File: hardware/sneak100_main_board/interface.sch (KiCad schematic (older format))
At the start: 18 parts, among them J11 USB_OTG, J12 Conn_01x06, J13 Conn_01x02, SW2 SW_Push, U8 TSOP4838

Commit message: Add OLED display
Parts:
- removed J13: Conn_01x02, Connector_PinHeader_2.54mm:PinHeader_1x02_P2.54mm_Vertical, symbol Connector_Generic:Conn_01x02
- added C17, C18: 100nF, Capacitor_SMD:C_0603_1608Metric, symbol Device:C
- added R21, R22: 4k7, Resistor_SMD:R_0603_1608Metric, symbol Device:R
- added SW3, SW4: SW_Push, Button_Switch_SMD:SW_SPST_FSMSM, symbol Switch:SW_Push
- renumbered C17 to C19, R21 to R23, R22 to R24, R23 to R25, R24 to R26, R25 to R27, R26 to R28
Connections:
- wire segments 17 -> 29
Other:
- note added: "user buttons"
- note removed: "user button"
- moved on the sheet: C16, R20, SW2

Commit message: delete USB, modify top hull, bigger PCB board
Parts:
- removed D11: LED, LED_SMD:LED_0603_1608Metric, symbol Device:LED
- removed J11: USB_OTG, Connector_USB:USB_Mini-B_Lumberg_2486_01_Horizontal, symbol Connector:USB_OTG
- removed R23, R24: 300, Resistor_SMD:R_0603_1608Metric, symbol Device:R
- removed R27, R28: 22, Resistor_SMD:R_0603_1608Metric, symbol Device:R
- added J12: Conn_01x04, Connector_PinHeader_2.54mm:PinHeader_1x04_P2.54mm_Vertical, symbol Connector_Generic:Conn_01x04
- added R26: 340, Resistor_SMD:R_0603_1608Metric, symbol Device:R
- SW2, SW3, SW4: footprint Button_Switch_SMD:SW_SPST_FSMSM -> Button_Switch_SMD:SW_Push_1P1T_NO_6x6mm_H9.5mm
- renumbered C16 to C27, C17 to C28, C18 to C29, C19 to C30, J12 to J13, R19 to R22, R20 to R23, R21 to R24, R22 to R25, R25 to R27, R26 to R28, U8 to U9
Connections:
- net labels added: BUTTON_C, BUTTON_L, BUTTON_R, LED_ERROR, LED_RUN
- net labels removed: BUTTON, LED1, LED2, LED3, USB_DM, USB_DP
- wire segments 29 -> 25
- no-connect marks 5 -> 2
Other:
- note added: "Green led current resistor calculations:\n\ntarget current: I = 5mA\ninput voltage: U = 3.3V\nforward voltage: Uf = 2V\n\nR = (U-Uf)/I\nR = (3.3 -2)/0.005 = 260ohm -> 300ohm"
- note added: "HC-05 module"
- note added: "OLED display"
- note added: "Red led current resistor calculations:\n\ntarget current: I = 5mA\ninput voltage: U = 3.3V\nforward voltage: Uf = 1.6V\n\nR = (U-Uf)/I\nR = (3.3 -1.6)/0.005 = 340ohm"
- note added: "SSD1306 module"
- note added: "user led"
- note removed: "For future use:\n- IMU\n- OLED display"
- note removed: "Green led current resistor calculations:\n\ntarget current: I = 5mA\ninput voltage: U = 3.3V\nforward voltage: Uf = 2V\n\nR = (U-Uf)/I\nR = (3.3 -2.9)/0.005 = 260ohm -> 300ohm"
- note removed: "I2C bus"
- note removed: "USB connection"
- note removed: "user leds"
- moved on the sheet: C27, C29, R23, R25, SW2, SW4

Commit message: Board interface layout
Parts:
- removed J12: Conn_01x04, Connector_PinHeader_2.54mm:PinHeader_1x04_P2.54mm_Vertical, symbol Connector_Generic:Conn_01x04
- added U10: SSD1306, sneak100_lib:SSD1306_module, symbol Sneak100_kicad:SSD1306
- renumbered D9 to D7, D10 to D8, J13 to J12, R22 to R18, R23 to R19, R24 to R20, R25 to R21, R26 to R22, R27 to R23, R28 to R24
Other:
- note removed: "SSD1306 module"
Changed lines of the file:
@@
 $EndComp
 $Comp
-L Device:R R23
+L Device:R R19
 U 1 1 61055001
 P 1700 1700
-F 0 "R23" H 1770 1746 50  0000 L CNN
+F 0 "R19" H 1770 1746 50  0000 L CNN
 F 1 "4k7" H 1770 1655 50  0000 L CNN
 F 2 "Resistor_SMD:R_0603_1608Metric" V 1630 1700 50  0001 C CNN
@@
 $EndComp
 $Comp
-L power:+3.3V #PWR0114
+L power:+3.3V #PWR0109
 U 1 1 610558C1
 P 1700 1550
-F 0 "#PWR0114" H 1700 1400 50  0001 C CNN
+F 0 "#PWR0109" H 1700 1400 50  0001 C CNN
 F 1 "+3.3V" H 1715 1723 50  0000 C CNN
 F 2 "" H 1700 1550 50  0001 C CNN
@@
 $EndComp
 $Comp
-L power:GND #PWR0118
+L power:GND #PWR0113
 U 1 1 61055FD5
 P 1200 1950
-F 0 "#PWR0118" H 1200 1700 50  0001 C CNN
+F 0 "#PWR0113" H 1200 1700 50  0001 C CNN
 F 1 "GND" H 1205 1777 50  0000 C CNN
 F 2 "" H 1200 1950 50  0001 C CNN
@@
 $EndComp
 $Comp
-L power:GND #PWR0122
+L power:GND #PWR0117
 U 1 1 6105698D
 P 1700 2250
-F 0 "#PWR0122" H 1700 2000 50  0001 C CNN
+F 0 "#PWR0117" H 1700 2000 50  0001 C CNN
 F 1 "GND" H 1705 2077 50  0000 C CNN
 F 2 "" H 1700 2250 50  0001 C CNN
@@
 BUTTON_L
 $Comp
-L Device:LED D9
+L Device:LED D7
 U 1 1 6105F07D
 P 6450 1650
-F 0 "D9" H 6443 1395 50  0000 C CNN
+F 0 "D7" H 6443 1395 50  0000 C CNN
 F 1 "LED" H 6443 1486 50  0000 C CNN
 F 2 "LED_SMD:LED_0603_1608Metric" H 6450 1650 50  0001 C CNN
@@
 $EndComp
 $Comp
-L Device:R R22
+L Device:R R18
 U 1 1 61060DB0
 P 6150 1650
-F 0 "R22" V 5943 1650 50  0000 C CNN
+F 0 "R18" V 5943 1650 50  0000 C CNN
 F 1 "300" V 6034 1650 50  0000 C CNN
 F 2 "Resistor_SMD:R_0603_1608Metric" V 6080 1650 50  0001 C CNN
@@
 $EndComp
 $Comp
-L power:GND #PWR0117
+L power:GND #PWR0112
 U 1 1 61061E6F
 P 6600 1650
-F 0 "#PWR0117" H 6600 1400 50  0001 C CNN
+F 0 "#PWR0112" H 6600 1400 50  0001 C CNN
 F 1 "GND" V 6605 1522 50  0000 R CNN
 F 2 "" H 6600 1650 50  0001 C CNN
@@
 bluetooth module
 $Comp
-L Connector_Generic:Conn_01x06 J13
+L Connector_Generic:Conn_01x06 J12
 U 1 1 60F1EA00
 P 2350 6150
-F 0 "J13" H 2430 6142 50  0000 L CNN
+F 0 "J12" H 2430 6142 50  0000 L CNN
 F 1 "Conn_01x06" H 2430 6051 50  0000 L CNN
 F 2 "Connector_PinSocket_2.54mm:PinSocket_1x06_P2.54mm_Vertical" H 2350 6150 50  0001 C CNN
@@
 BLUETOOTH_TX
 $Comp
-L power:GND #PWR0133
+L power:GND #PWR0128
 U 1 1 60F1FEEB
 P 2150 6150
-F 0 "#PWR0133" H 2150 5900 50  0001 C CNN
+F 0 "#PWR0128" H 2150 5900 50  0001 C CNN
 F 1 "GND" V 2155 6022 50  0000 R CNN
 F 2 "" H 2150 6150 50  0001 C CNN
@@
 $EndComp
 $Comp
-L power:+5V #PWR0131
+L power:+5V #PWR0125
 U 1 1 60F200B0
 P 2150 6050
-F 0 "#PWR0131" H 2150 5900 50  0001 C CNN
+F 0 "#PWR0125" H 2150 5900 50  0001 C CNN
 F 1 "+5V" V 2165 6178 50  0000 L CNN
 F 2 "" H 2150 6050 50  0001 C CNN
@@
 Text Notes 5500 5500 0    100  ~ 20
 OLED display
-Text HLabel 5900 6300 0    50   BiDi ~ 0
+Text HLabel 6200 6050 1    50   BiDi ~ 0
 I2C_SDA
-Text HLabel 5900 6200 0    50   BiDi ~ 0
+Text HLabel 6100 6050 1    50   BiDi ~ 0
 I2C_SCL
 Text Notes 6200 3250 0    100  ~ 20
@@
 $EndComp
 $Comp
-L power:GND #PWR0129
+L power:GND #PWR0124
 U 1 1 60F7CCD5
 P 7150 4450
-F 0 "#PWR0129" H 7150 4200 50  0001 C CNN
+F 0 "#PWR0124" H 7150 4200 50  0001 C CNN
 F 1 "GND" H 7155 4277 50  0000 C CNN
 F 2 "" H 7150 4450 50  0001 C CNN
@@
 $EndComp
 $Comp
-L power:+3.3V #PWR0127
+L power:+3.3V #PWR0122
 U 1 1 60F7DC2F
 P 7450 3650
-F 0 "#PWR0127" H 7450 3500 50  0001 C CNN
+F 0 "#PWR0122" H 7450 3500 50  0001 C CNN
 F 1 "+3.3V" H 7465 3823 50  0000 C CNN
 F 2 "" H 7450 3650 50  0001 C CNN
@@
 $EndComp
 $Comp
-L power:GND #PWR0128
+L power:GND #PWR0123
 U 1 1 60F80FC7
 P 5900 3950
-F 0 "#PWR0128" H 5900 3700 50  0001 C CNN
+F 0 "#PWR0123" H 5900 3700 50  0001 C CNN
 F 1 "GND" H 5905 3777 50  0000 C CNN
 F 2 "" H 5900 3950 50  0001 C CNN
@@
 $EndComp
 $Comp
-L power:+3.3V #PWR0125
+L power:+3.3V #PWR0120
 U 1 1 60F81378
 P 5900 3650
-F 0 "#PWR0125" H 5900 3500 50  0001 C CNN
+F 0 "#PWR0120" H 5900 3500 50  0001 C CNN
 F 1 "+3.3V" H 5915 3823 50  0000 C CNN
 F 2 "" H 5900 3650 50  0001 C CNN
@@
 $EndComp
 $Comp
-L Device:R R27
+L Device:R R23
 U 1 1 60F8B46D
 P 7150 3800
-F 0 "R27" H 7220 3846 50  0000 L CNN
+F 0 "R23" H 7220 3846 50  0000 L CNN
 F 1 "100" H 7220 3755 50  0000 L CNN
 F 2 "Resistor_SMD:R_0603_1608Metric" V 7080 3800 50  0001 C CNN
@@
 $EndComp
 $Comp
-L power:+3.3V #PWR0126
+L power:+3.3V #PWR0121
 U 1 1 60F8BCE9
 P 7150 3650
-F 0 "#PWR0126" H 7150 3500 50  0001 C CNN
+F 0 "#PWR0121" H 7150 3500 50  0001 C CNN
 F 1 "+3.3V" H 7165 3823 50  0000 C CNN
 F 2 "" H 7150 3650 50  0001 C CNN
@@
 	7150 4400 7150 4450
 $Comp
-L Device:R R28
+L Device:R R24
 U 1 1 60F9B98E
 P 7450 3800
-F 0 "R28" H 7520 3846 50  0000 L CNN
+F 0 "R24" H 7520 3846 50  0000 L CNN
 F 1 "10k" H 7520 3755 50  0000 L CNN
 F 2 "Resistor_SMD:R_0603_1608Metric" V 7380 3800 50  0001 C CNN
@@
 $EndComp
 $Comp
-L Device:R R24
+L Device:R R20
 U 1 1 60F90EC5
 P 2900 1700
-F 0 "R24" H 2970 1746 50  0000 L CNN
+F 0 "R20" H 2970 1746 50  0000 L CNN
 F 1 "4k7" H 2970 1655 50  0000 L CNN
 F 2 "Resistor_SMD:R_0603_1608Metric" V 2830 1700 50  0001 C CNN
@@
 $EndComp
 $Comp
-L power:+3.3V #PWR0115
+L power:+3.3V #PWR0110
 U 1 1 60F90ECB
 P 2900 1550
-F 0 "#PWR0115" H 2900 1400 50  0001 C CNN
+F 0 "#PWR0110" H 2900 1400 50  0001 C CNN
 F 1 "+3.3V" H 2915 1723 50  0000 C CNN
 F 2 "" H 2900 1550 50  0001 C CNN
@@
 $EndComp
 $Comp
-L power:GND #PWR0119
+L power:GND #PWR0114
 U 1 1 60F90ED1
 P 2400 1950
-F 0 "#PWR0119" H 2400 1700 50  0001 C CNN
+F 0 "#PWR0114" H 2400 1700 50  0001 C CNN
 F 1 "GND" H 2405 1777 50  0000 C CNN
 F 2 "" H 2400 1950 50  0001 C CNN
@@
 $EndComp
 $Comp
-L power:GND #PWR0123
+L power:GND #PWR0118
 U 1 1 60F90EDD
 P 2900 2250
-F 0 "#PWR0123" H 2900 2000 50  0001 C CNN
+F 0 "#PWR0118" H 2900 2000 50  0001 C CNN
 F 1 "GND" H 2905 2077 50  0000 C CNN
 F 2 "" H 2900 2250 50  0001 C CNN
@@
 $EndComp
 $Comp
-L Device:R R25
+L Device:R R21
 U 1 1 60F92AB2
 P 4100 1700
-F 0 "R25" H 4170 1746 50  0000 L CNN
+F 0 "R21" H 4170 1746 50  0000 L CNN
 F 1 "4k7" H 4170 1655 50  0000 L CNN
 F 2 "Resistor_SMD:R_0603_1608Metric" V 4030 1700 50  0001 C CNN
@@
 $EndComp
 $Comp
-L power:+3.3V #PWR0116
+L power:+3.3V #PWR0111
 U 1 1 60F92AB8
 P 4100 1550
-F 0 "#PWR0116" H 4100 1400 50  0001 C CNN
+F 0 "#PWR0111" H 4100 1400 50  0001 C CNN
 F 1 "+3.3V" H 4115 1723 50  0000 C CNN
 F 2 "" H 4100 1550 50  0001 C CNN
@@
 $EndComp
 $Comp
-L power:GND #PWR0120
+L power:GND #PWR0115
 U 1 1 60F92ABE
 P 3600 1950
-F 0 "#PWR0120" H 3600 1700 50  0001 C CNN
+F 0 "#PWR0115" H 3600 1700 50  0001 C CNN
 F 1 "GND" H 3605 1777 50  0000 C CNN
 F 2 "" H 3600 1950 50  0001 C CNN
@@
 $EndComp
 $Comp
-L power:GND #PWR0124
+L power:GND #PWR0119
 U 1 1 60F92ACA
 P 4100 2250
-F 0 "#PWR0124" H 4100 2000 50  0001 C CNN
+F 0 "#PWR0119" H 4100 2000 50  0001 C CNN
 F 1 "GND" H 4105 2077 50  0000 C CNN
 F 2 "" H 4100 2250 50  0001 C CNN
@@
 BUTTON_R
 $Comp
-L Connector_Generic:Conn_01x04 J12
-U 1 1 60FBB3CA
-P 6100 6100
-F 0 "J12" H 6180 6092 50  0000 L CNN
-F 1 "Conn_01x04" H 6180 6001 50  0000 L CNN
-F 2 "Connector_PinHeader_2.54mm:PinHeader_1x04_P2.54mm_Vertical" H 6100 6100 50  0001 C CNN
-F 3 "~" H 6100 6100 50  0001 C CNN
-	1    6100 6100
-	1    0    0    -1
-$EndComp
-$Comp
-L power:+3.3V #PWR0130
+L power:+3.3V #PWR0126
 U 1 1 60FBF32E
-P 5900 6000
-F 0 "#PWR0130" H 5900 5850 50  0001 C CNN
-F 1 "+3.3V" V 5915 6128 50  0000 L CNN
-F 2 "" H 5900 6000 50  0001 C CNN
-F 3 "" H 5900 6000 50  0001 C CNN
-	1    5900 6000
-	0    -1   -1   0
-$EndComp
-$Comp
-L power:GND #PWR0132
+P 5900 6050
+F 0 "#PWR0126" H 5900 5900 50  0001 C CNN
+F 1 "+3.3V" V 5915 6178 50  0000 L CNN
+F 2 "" H 5900 6050 50  0001 C CNN
+F 3 "" H 5900 6050 50  0001 C CNN
+	1    5900 6050
+	1    0    0    -1
+$EndComp
+$Comp
+L power:GND #PWR0127
 U 1 1 60FBFC20
-P 5900 6100
-F 0 "#PWR0132" H 5900 5850 50  0001 C CNN
-F 1 "GND" V 5905 5972 50  0000 R CNN
-F 2 "" H 5900 6100 50  0001 C CNN
-F 3 "" H 5900 6100 50  0001 C CNN
-	1    5900 6100
-	0    1    1    0
-$EndComp
-$Comp
-L Device:LED D10
+P 6000 6050
+F 0 "#PWR0127" H 6000 5800 50  0001 C CNN
+F 1 "GND" V 6005 5922 50  0000 R CNN
+F 2 "" H 6000 6050 50  0001 C CNN
+F 3 "" H 6000 6050 50  0001 C CNN
+	1    6000 6050
+	-1   0    0    1
+$EndComp
+$Comp
+L Device:LED D8
 U 1 1 60FD241C
 P 6450 2100
-F 0 "D10" H 6443 1845 50  0000 C CNN
+F 0 "D8" H 6443 1845 50  0000 C CNN
 F 1 "LED" H 6443 1936 50  0000 C CNN
 F 2 "LED_SMD:LED_0603_1608Metric" H 6450 2100 50  0001 C CNN
@@
 $EndComp
 $Comp
-L Device:R R26
+L Device:R R22
 U 1 1 60FD2422
 P 6150 2100
-F 0 "R26" V 5943 2100 50  0000 C CNN
+F 0 "R22" V 5943 2100 50  0000 C CNN
 F 1 "340" V 6034 2100 50  0000 C CNN
 F 2 "Resistor_SMD:R_0603_1608Metric" V 6080 2100 50  0001 C CNN
@@
 $EndComp
 $Comp
-L power:GND #PWR0121
+L power:GND #PWR0116
 U 1 1 60FD2428
 P 6600 2100
-F 0 "#PWR0121" H 6600 1850 50  0001 C CNN
+F 0 "#PWR0116" H 6600 1850 50  0001 C CNN
 F 1 "GND" V 6605 1972 50  0000 R CNN
 F 2 "" H 6600 2100 50  0001 C CNN
@@
 Text Notes 7600 2550 0    50   ~ 0
 Red led current resistor calculations:\n\ntarget current: I = 5mA\ninput voltage: U = 3.3V\nforward voltage: Uf = 1.6V\n\nR = (U-Uf)/I\nR = (3.3 -1.6)/0.005 = 340ohm
-Text Notes 5650 5650 0    50   ~ 10
-SSD1306 module
 Text Notes 2000 5600 0    50   ~ 10
 HC-05 module
+$Comp
+L Sneak100_kicad:SSD1306 U10
+U 1 1 6101ACF5
+P 6050 6400
+F 0 "U10" H 6650 6750 50  0000 R CNN
+F 1 "SSD1306" H 6800 6650 50  0000 R CNN
+F 2 "sneak100_lib:SSD1306_module" H 5900 6350 50  0001 C CNN
+F 3 "" H 5900 6350 50  0001 C CNN
+	1    6050 6400
+	1    0    0    -1
+$EndComp
 $EndSCHEMATC

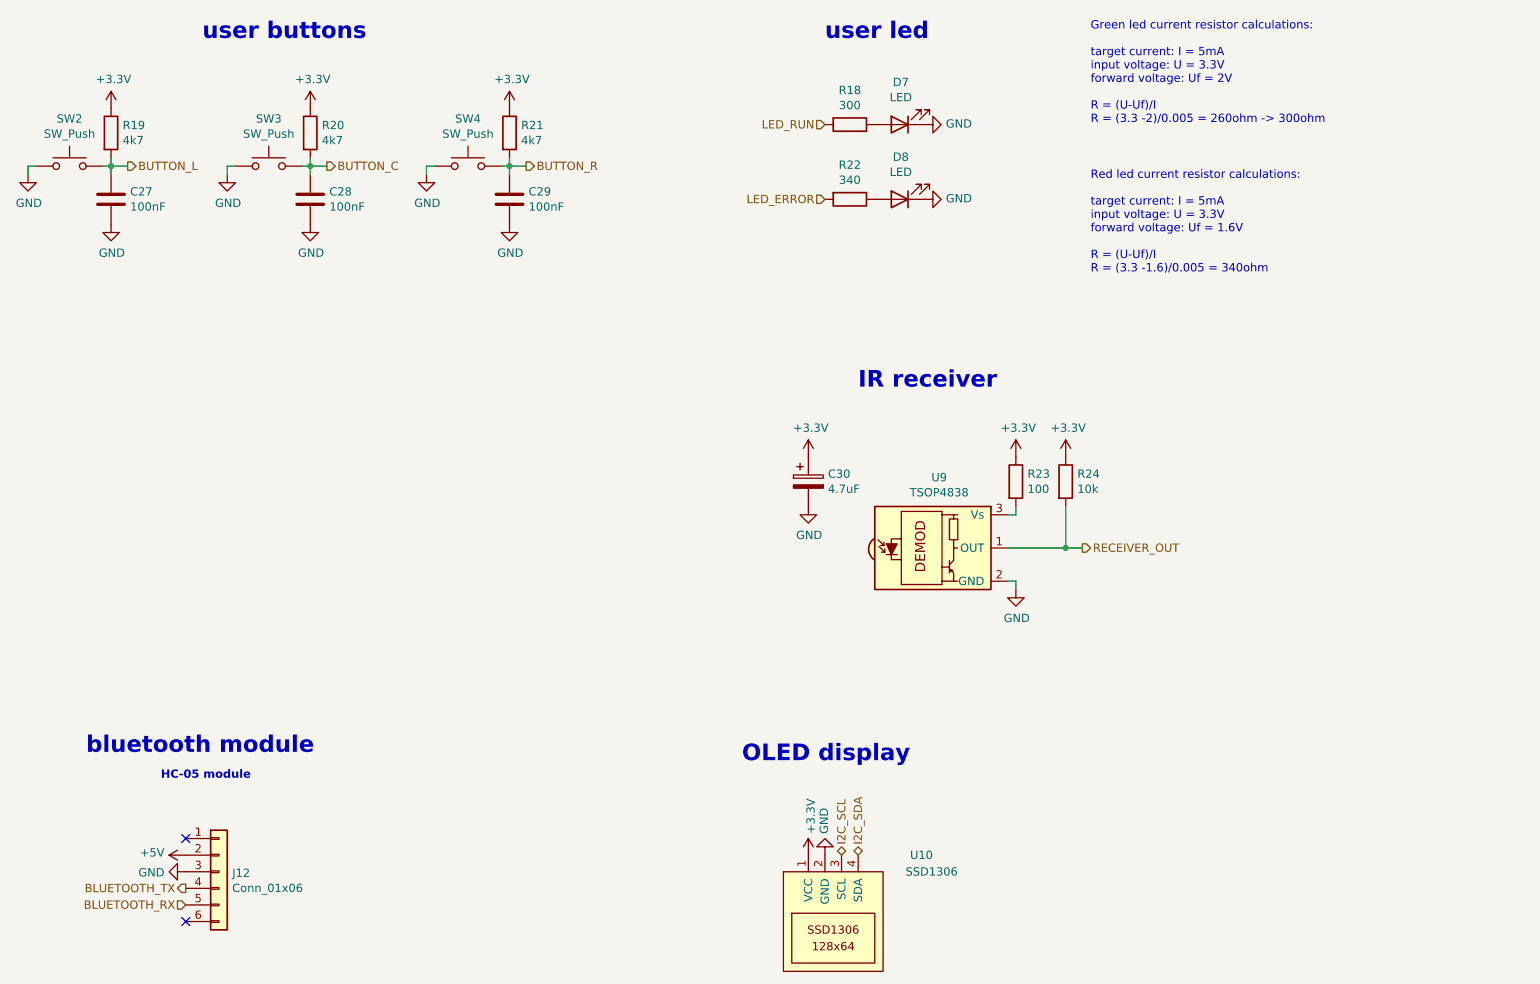
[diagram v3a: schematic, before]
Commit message: PCB first full layout
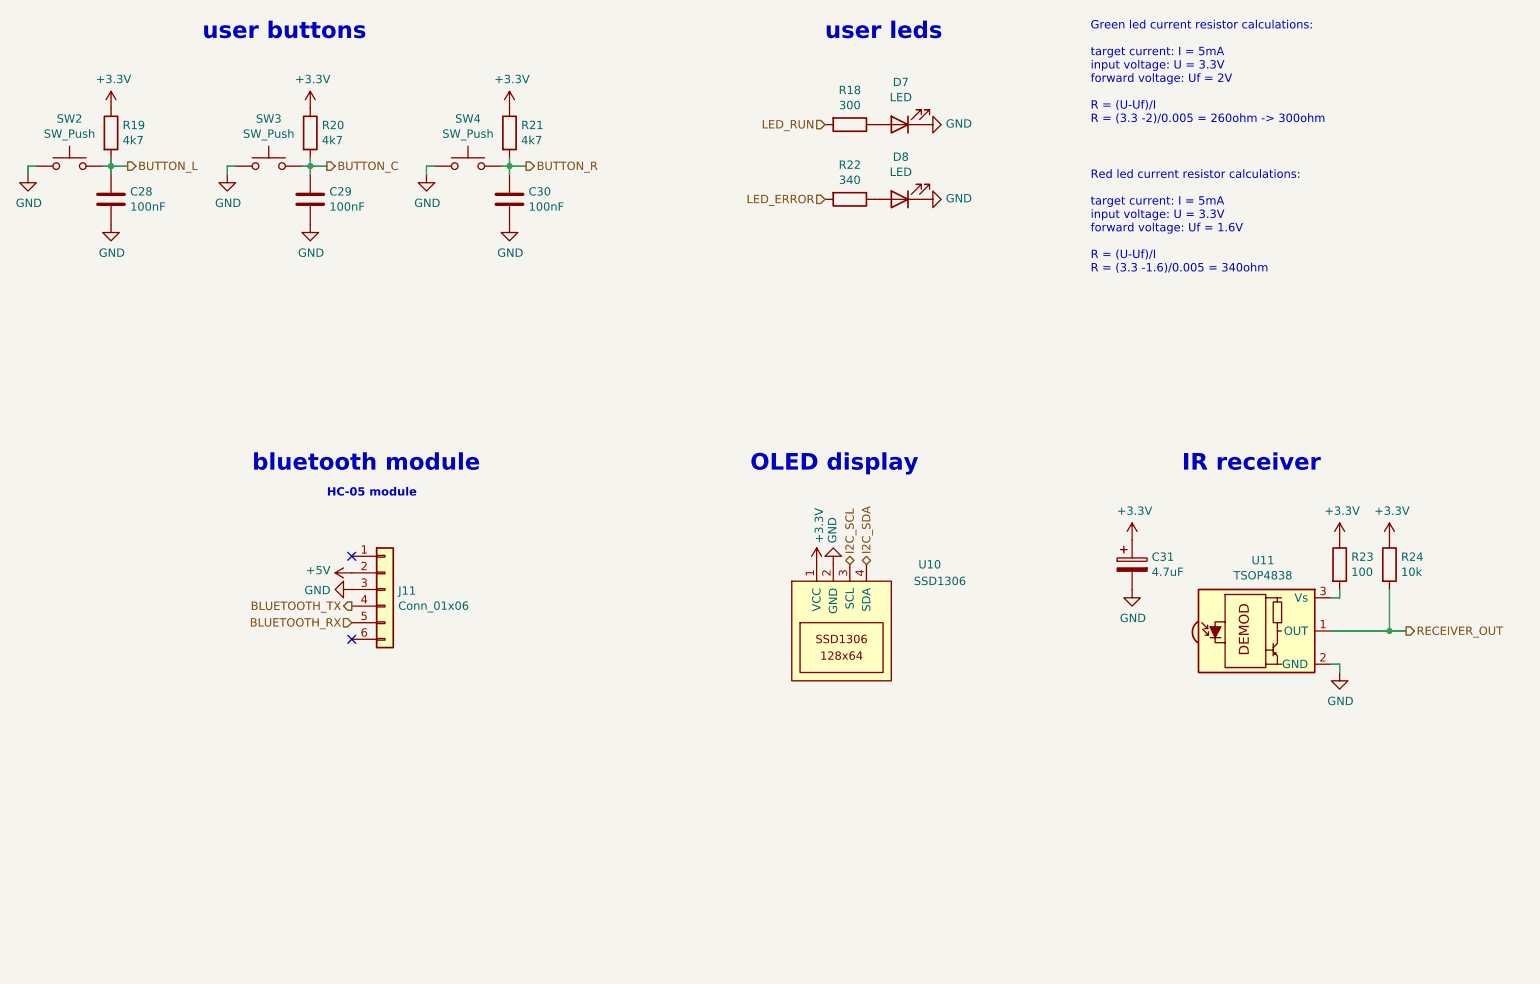
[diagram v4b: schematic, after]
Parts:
- renumbered C27 to C28, C28 to C29, C29 to C30, C30 to C31, J12 to J11, U9 to U11
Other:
- note added: "user leds"
- note removed: "user led"
- moved on the sheet: C31, J11, R23, R24, U10, U11
